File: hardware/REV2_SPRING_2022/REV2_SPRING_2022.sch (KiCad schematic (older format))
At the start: 38 parts, among them J101 Screw_Terminal_01x02, J102 Screw_Terminal_01x02, J103 Conn_01x02_Female, J104 Screw_Terminal_01x02, J105 Conn_01x02_Female, J106 Conn_01x02_Female, J107 Screw_Terminal_01x02, J108 Screw_Terminal_01x02, J109 Conn_01x02_Female, J110 Conn_01x02_Female, Q101 Q_NMOS_GDS, Q102 Q_NMOS_GDS, U1 Teensy3.6_All_Pins, U2 PA16165_Breakout, U3 MPL3115A2_Breakout, U4 BNO055_Breakout, U5 RFM69HCW_Breakout

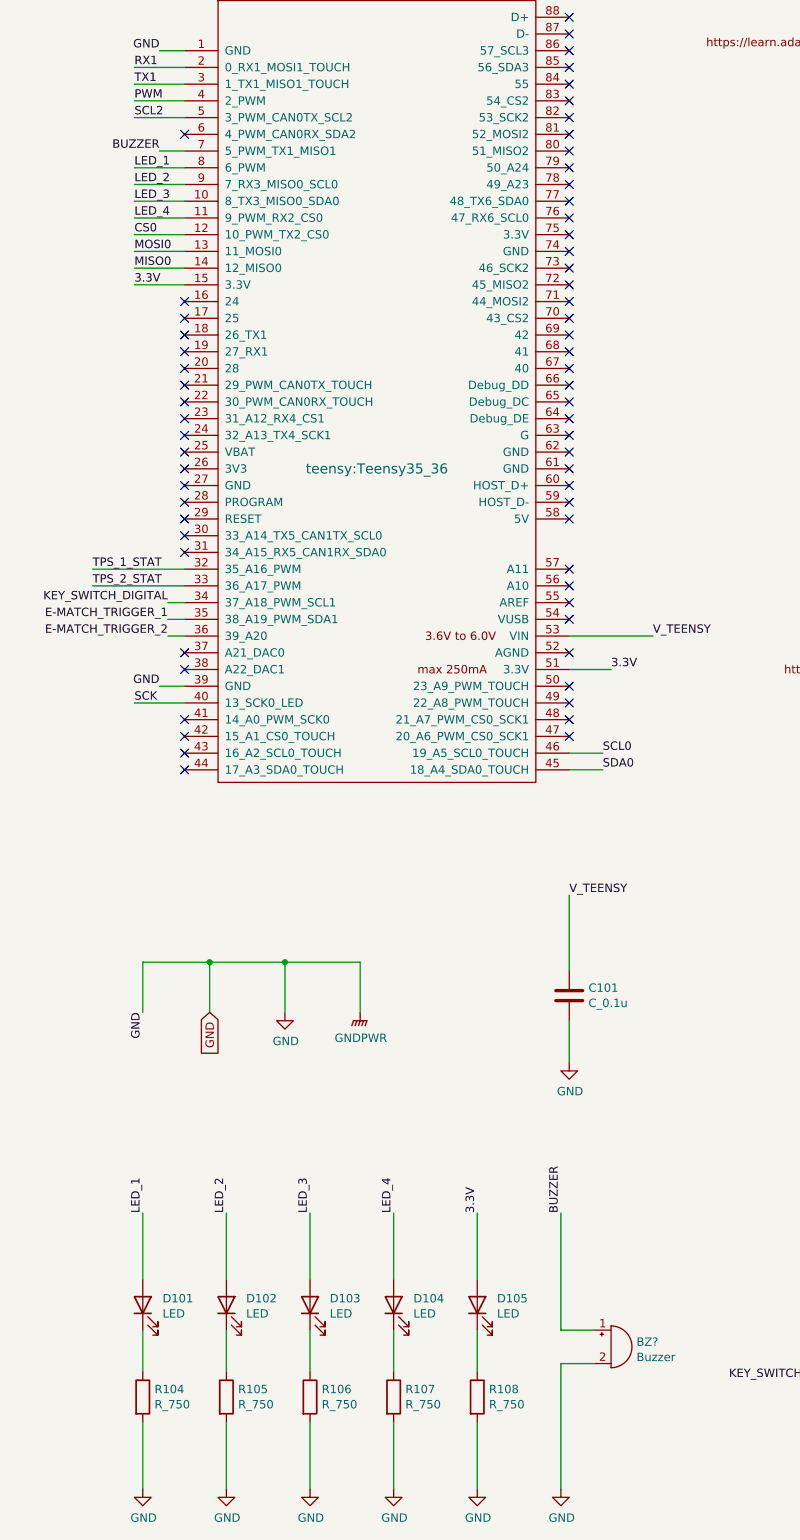
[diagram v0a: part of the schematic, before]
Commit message: add another LED to schematic and layout
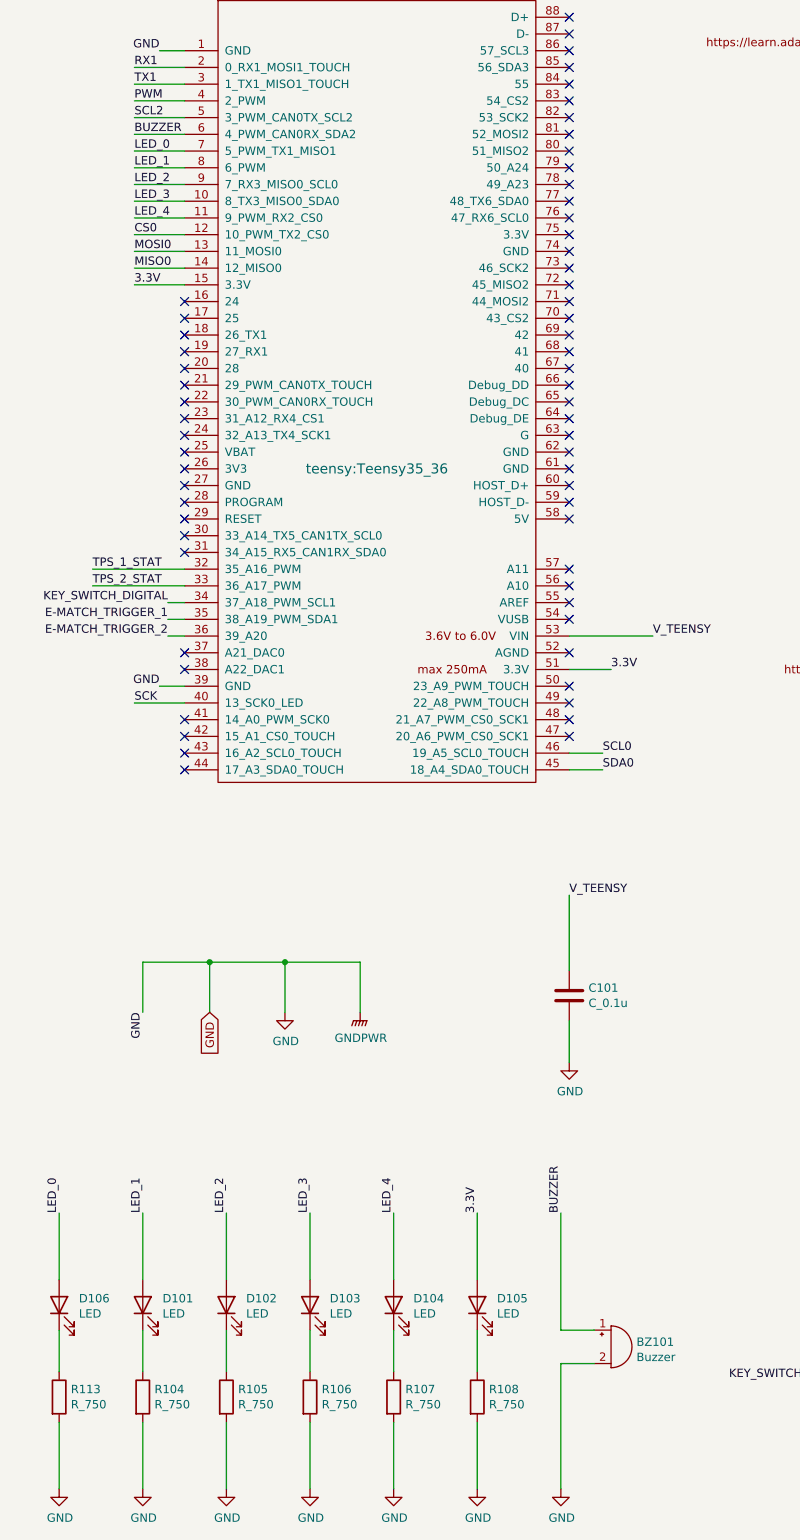
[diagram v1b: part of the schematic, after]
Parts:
- added D106: LED, LED_SMD:LED_0805_2012Metric_Pad1.15x1.40mm_HandSolder, symbol Device:LED
- added R113: R_750, Resistor_SMD:R_0805_2012Metric_Pad1.20x1.40mm_HandSolder, symbol Device:R
- gave numbers to parts that had none: 1
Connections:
- net BUZZER: now also U1.6 (4_PWM_CAN0RX_SDA2); no longer U1.7 (5_PWM_TX1_MISO1)
- net GND: now also R113.2
- new net: D106.1 (K), R113.1
- new net LED_0: D106.2 (A), U1.7 (5_PWM_TX1_MISO1)
- no-connect marks 83 -> 82
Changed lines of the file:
@@
 Wire Wire Line
 	8400 2850 8700 2850
-NoConn ~ 1450 1950
 NoConn ~ 1450 2950
 NoConn ~ 1450 3050
@@
 KEY_SWITCH_DIGITAL
 $Comp
-L Device:Buzzer BZ?
+L Device:Buzzer BZ101
 U 1 1 61F00FB7
 P 4000 9200
-F 0 "BZ?" H 4152 9229 50  0000 L CNN
+F 0 "BZ101" H 4152 9229 50  0000 L CNN
 F 1 "Buzzer" H 4152 9138 50  0000 L CNN
 F 2 "Olin_Rocketry:Large_Buzzer_24mmOD_14.8mmPinDistance_1.0mmPinDiameter" V 3975 9300 50  0001 C CNN
@@
 	3700 9300 3700 10050
 $Comp
-L power:GND #PWR?
+L power:GND #PWR0116
 U 1 1 61F0EB81
 P 3700 10050
-F 0 "#PWR?" H 3700 9800 50  0001 C CNN
+F 0 "#PWR0116" H 3700 9800 50  0001 C CNN
 F 1 "GND" H 3705 9877 50  0000 C CNN
 F 2 "" H 3700 10050 50  0001 C CNN
@@
 Text Label 3700 8400 1    50   ~ 0
 BUZZER
-Text Label 1300 2050 2    50   ~ 0
+Text Label 1150 1950 0    50   ~ 0
 BUZZER
 Wire Wire Line
-	1450 2050 1300 2050
+	1450 2050 1150 2050
+$Comp
+L Device:LED D106
+U 1 1 61F1A35A
+P 700 8950
+F 0 "D106" V 739 8832 50  0000 R CNN
+F 1 "LED" V 648 8832 50  0000 R CNN
+F 2 "LED_SMD:LED_0805_2012Metric_Pad1.15x1.40mm_HandSolder" H 700 8950 50  0001 C CNN
+F 3 "https://datasheet.lcsc.com/lcsc/1806130620_Hubei-KENTO-Elec-C2293_C2293.pdf" H 700 8950 50  0001 C CNN
+	1    700  8950
+	0    -1   -1   0
+$EndComp
+$Comp
+L Device:R R113
+U 1 1 61F1A360
+P 700 9500
+F 0 "R113" H 770 9546 50  0000 L CNN
+F 1 "R_750" H 770 9455 50  0000 L CNN
+F 2 "Resistor_SMD:R_0805_2012Metric_Pad1.20x1.40mm_HandSolder" V 630 9500 50  0001 C CNN
+F 3 "~" H 700 9500 50  0001 C CNN
+	1    700  9500
+	1    0    0    -1
+$EndComp
+Wire Wire Line
+	700  9100 700  9350
+Text Label 700  8400 1    50   ~ 0
+LED_0
+Wire Wire Line
+	700  8400 700  8800
+Wire Wire Line
+	700  9650 700  10050
+$Comp
+L power:GND #PWR0122
+U 1 1 61F1A36A
+P 700 10050
+F 0 "#PWR0122" H 700 9800 50  0001 C CNN
+F 1 "GND" H 705 9877 50  0000 C CNN
+F 2 "" H 700 10050 50  0001 C CNN
+F 3 "" H 700 10050 50  0001 C CNN
+	1    700  10050
+	1    0    0    -1
+$EndComp
+Text Label 1150 2050 0    50   ~ 0
+LED_0
+Wire Wire Line
+	1450 1950 1150 1950
 $EndSCHEMATC

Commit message: wip
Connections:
- net EMATCH_1+: now reaches J101.2 (Pin_2), J109.2 (Pin_2), Q101.2 (D), R111.2
- net EMATCH_2+: now reaches J102.2 (Pin_2), J110.2 (Pin_2), Q102.2 (D), R112.2
- net TPS2113A for E-match/IN1 renamed BAT1
- net TPS2113A for E-match/IN2 renamed BAT2
- net TPS2113A for E-match/VOUT renamed V_EMATCH_TO_KEY_SWITCH
- net TPS2113A for Teensy power/VOUT renamed VIN_TO_TEENSY_TO_KEY_SWITCH
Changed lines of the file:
@@
 Wire Wire Line
 	1450 1950 1150 1950
+Text Label 21050 3200 0    50   ~ 0
+EMATCH_1+
+Text Label 21050 6200 0    50   ~ 0
+EMATCH_2+
+Text Label 6250 8950 0    50   ~ 0
+KEY_SWITCH_DIGITAL_3V3
+Text Label 16250 2700 0    50   ~ 0
+V_EMATCH_TO_KEY_SWITCH
+Text Label 16200 5050 0    50   ~ 0
+VIN_TO_TEENSY_TO_KEY_SWITCH
+Text Label 13400 4350 0    50   ~ 0
+BAT1
+Text Label 13400 3500 0    50   ~ 0
+BAT2
 $EndSCHEMATC

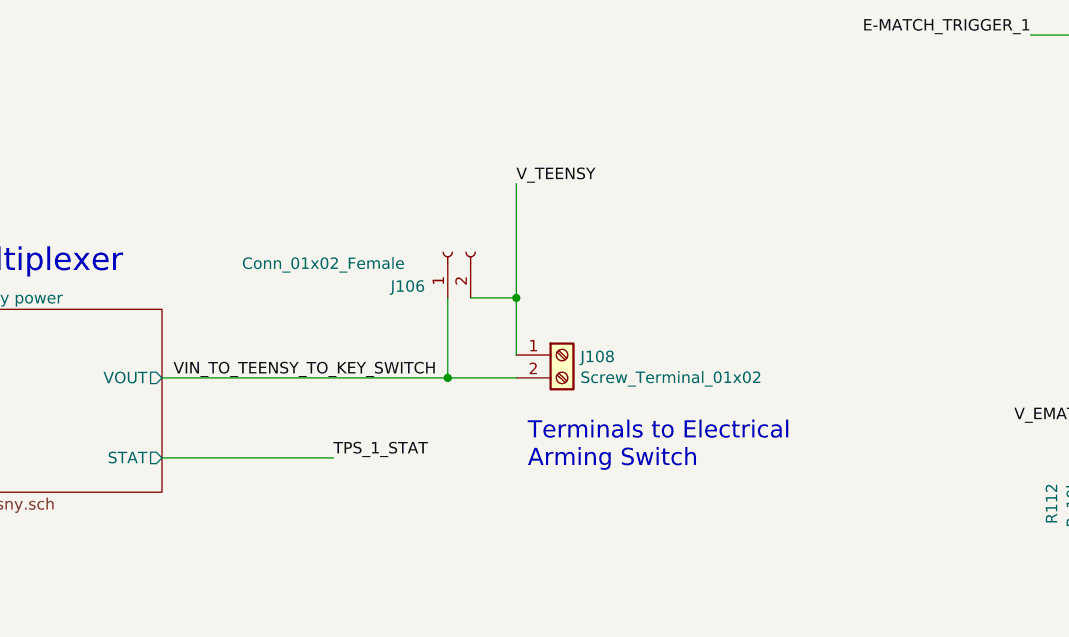
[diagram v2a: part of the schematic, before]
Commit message: remove hardware electrical arming (now using software arming)
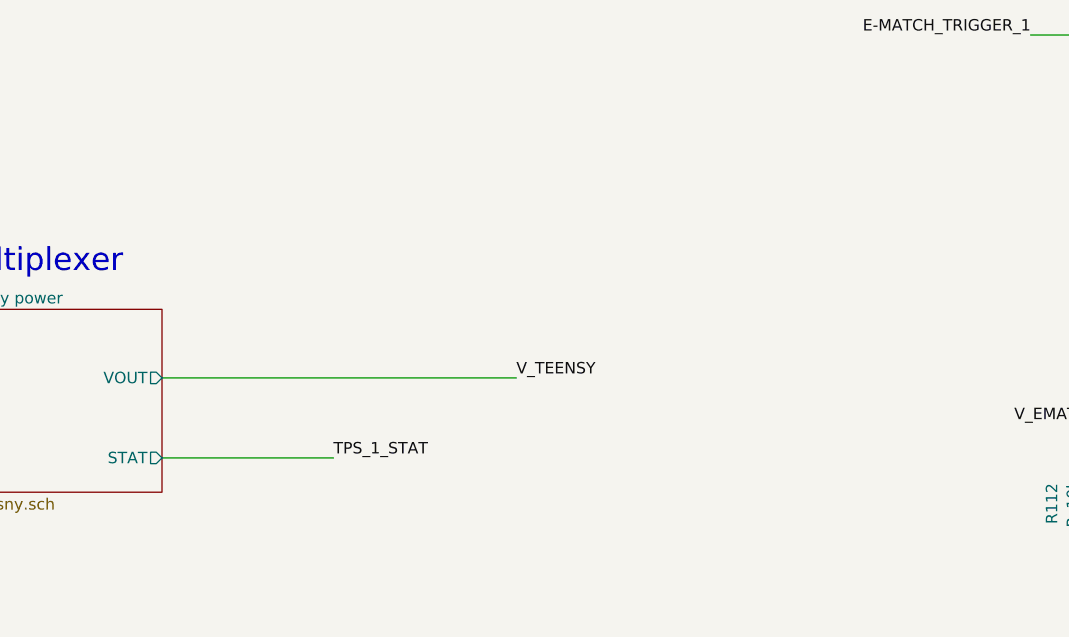
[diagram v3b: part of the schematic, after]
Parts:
- removed J106: Conn_01x02_Female, Connector_Wire:SolderWire-1sqmm_1x02_P5.4mm_D1.4mm_OD2.7mm_Relief2x, symbol Connector:Conn_01x02_Female
- removed J108: Screw_Terminal_01x02, TerminalBlock:TerminalBlock_bornier-2_P5.08mm, symbol Connector:Screw_Terminal_01x02
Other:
- note removed: "Terminals to Electrical \nArming Switch"
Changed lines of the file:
@@
 	0    1    1    0
 $EndComp
-Text Label 17700 4200 0    50   ~ 0
+Text Label 17700 5050 0    50   ~ 0
 V_TEENSY
 Text Label 17700 2050 0    50   ~ 0
@@
 Text Notes 17750 3050 0    75   ~ 0
 Terminals to Electromechanical \nArming Switch
-$Comp
-L Connector:Screw_Terminal_01x02 J108
-U 1 1 61BB7A24
-P 17900 4950
-F 0 "J108" H 17980 4942 50  0000 L CNN
-F 1 "Screw_Terminal_01x02" H 17980 4851 50  0000 L CNN
-F 2 "TerminalBlock:TerminalBlock_bornier-2_P5.08mm" H 17900 4950 50  0001 C CNN
-F 3 "~" H 17900 4950 50  0001 C CNN
-	1    17900 4950
-	1    0    0    -1
-$EndComp
-Wire Wire Line
-	16150 5050 17400 5050
-Wire Wire Line
-	17700 4950 17700 4700
-Text Notes 17750 5450 0    75   ~ 0
-Terminals to Electrical \nArming Switch
 Text Notes 14700 2250 0    100  ~ 0
 Power Multiplexer
@@
 	17400 2700 17700 2700
 $Comp
-L Connector:Conn_01x02_Female J106
-U 1 1 61EF490E
-P 17400 4500
-F 0 "J106" V 17250 4750 50  0000 R CNN
-F 1 "Conn_01x02_Female" V 17350 5400 50  0000 R CNN
-F 2 "Connector_Wire:SolderWire-1sqmm_1x02_P5.4mm_D1.4mm_OD2.7mm_Relief2x" H 17400 4500 50  0001 C CNN
-F 3 "~" H 17400 4500 50  0001 C CNN
-	1    17400 4500
-	0    -1   -1   0
-$EndComp
-Wire Wire Line
-	17500 4700 17700 4700
-Connection ~ 17700 4700
-Wire Wire Line
-	17700 4700 17700 4200
-Wire Wire Line
-	17400 4700 17400 5050
-Connection ~ 17400 5050
-Wire Wire Line
-	17400 5050 17700 5050
-$Comp
 L Device:R R111
 U 1 1 61EFFA45
@@
 Text Label 16250 2700 0    50   ~ 0
 V_EMATCH_TO_KEY_SWITCH
-Text Label 16200 5050 0    50   ~ 0
-VIN_TO_TEENSY_TO_KEY_SWITCH
 Text Label 13400 4350 0    50   ~ 0
 BAT1
 Text Label 13400 3500 0    50   ~ 0
 BAT2
+Wire Wire Line
+	16150 5050 17700 5050
 $EndSCHEMATC

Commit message: wip switch wire terminals
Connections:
- net EMATCH_1+: now also J101.1 (Pin_1), J109.1 (Pin_1); no longer J101.2 (Pin_2), J109.2 (Pin_2)
- net EMATCH_2+: now also J102.1 (Pin_1), J110.1 (Pin_1); no longer J102.2 (Pin_2), J110.2 (Pin_2)
- net V_EMATCH: now also J101.2 (Pin_2), J102.2 (Pin_2), J107.2 (Pin_2), J109.2 (Pin_2), J110.2 (Pin_2); no longer J101.1 (Pin_1), J102.1 (Pin_1), J107.1 (Pin_1), J109.1 (Pin_1), J110.1 (Pin_1)
- net V_EMATCH_TO_KEY_SWITCH: now also J107.1 (Pin_1); no longer J107.2 (Pin_2)
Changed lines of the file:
@@
 L Connector:Screw_Terminal_01x02 J102
 U 1 1 619F16C4
-P 21750 5600
-F 0 "J102" H 21830 5592 50  0000 L CNN
-F 1 "Screw_Terminal_01x02" H 21830 5501 50  0000 L CNN
-F 2 "TerminalBlock:TerminalBlock_bornier-2_P5.08mm" H 21750 5600 50  0001 C CNN
-F 3 "~" H 21750 5600 50  0001 C CNN
-	1    21750 5600
-	1    0    0    -1
+P 21750 5700
+F 0 "J102" H 21830 5692 50  0000 L CNN
+F 1 "Screw_Terminal_01x02" H 21830 5601 50  0000 L CNN
+F 2 "TerminalBlock:TerminalBlock_bornier-2_P5.08mm" H 21750 5700 50  0001 C CNN
+F 3 "~" H 21750 5700 50  0001 C CNN
+	1    21750 5700
+	1    0    0    1
 $EndComp
 Wire Wire Line
@@
 L Connector:Screw_Terminal_01x02 J107
 U 1 1 61BAEBD9
-P 17900 2600
-F 0 "J107" H 17980 2592 50  0000 L CNN
-F 1 "Screw_Terminal_01x02" H 17980 2501 50  0000 L CNN
-F 2 "TerminalBlock:TerminalBlock_bornier-2_P5.08mm" H 17900 2600 50  0001 C CNN
-F 3 "~" H 17900 2600 50  0001 C CNN
-	1    17900 2600
-	1    0    0    -1
+P 17900 2700
+F 0 "J107" H 17980 2692 50  0000 L CNN
+F 1 "Screw_Terminal_01x02" H 17980 2601 50  0000 L CNN
+F 2 "TerminalBlock:TerminalBlock_bornier-2_P5.08mm" H 17900 2700 50  0001 C CNN
+F 3 "~" H 17900 2700 50  0001 C CNN
+	1    17900 2700
+	1    0    0    1
 $EndComp
 Wire Wire Line
@@
 Wire Wire Line
 	14350 3050 14700 3050
-$Comp
-L Connector:Conn_01x02_Female J105
-U 1 1 61EE6B30
-P 17400 2150
-F 0 "J105" V 17250 2400 50  0000 R CNN
-F 1 "Conn_01x02_Female" V 17350 3050 50  0000 R CNN
-F 2 "Connector_Wire:SolderWire-1sqmm_1x02_P5.4mm_D1.4mm_OD2.7mm_Relief2x" H 17400 2150 50  0001 C CNN
-F 3 "~" H 17400 2150 50  0001 C CNN
-	1    17400 2150
-	0    -1   -1   0
-$EndComp
 Wire Wire Line
 	17500 2350 17700 2350
@@
 L Connector:Conn_01x02_Female J110
 U 1 1 61F21E7F
-P 21600 5150
-F 0 "J110" V 21450 4850 50  0000 R CNN
-F 1 "Conn_01x02_Female" V 21600 4850 50  0000 R CNN
-F 2 "Connector_Wire:SolderWire-1sqmm_1x02_P5.4mm_D1.4mm_OD2.7mm_Relief2x" H 21600 5150 50  0001 C CNN
-F 3 "~" H 21600 5150 50  0001 C CNN
-	1    21600 5150
-	0    -1   -1   0
+P 21700 5150
+F 0 "J110" V 21600 5400 50  0000 R CNN
+F 1 "Conn_01x02_Female" V 21700 6000 50  0000 R CNN
+F 2 "Connector_Wire:SolderWire-1sqmm_1x02_P5.4mm_D1.4mm_OD2.7mm_Relief2x" H 21700 5150 50  0001 C CNN
+F 3 "~" H 21700 5150 50  0001 C CNN
+	1    21700 5150
+	0    1    -1   0
 $EndComp
 Wire Wire Line
@@
 L Connector:Conn_01x02_Female J109
 U 1 1 61F16DD4
-P 21600 2150
-F 0 "J109" V 21450 1850 50  0000 R CNN
-F 1 "Conn_01x02_Female" V 21600 1850 50  0000 R CNN
-F 2 "Connector_Wire:SolderWire-1sqmm_1x02_P5.4mm_D1.4mm_OD2.7mm_Relief2x" H 21600 2150 50  0001 C CNN
-F 3 "~" H 21600 2150 50  0001 C CNN
-	1    21600 2150
-	0    -1   -1   0
+P 21700 2150
+F 0 "J109" V 21550 2400 50  0000 R CNN
+F 1 "Conn_01x02_Female" V 21700 3000 50  0000 R CNN
+F 2 "Connector_Wire:SolderWire-1sqmm_1x02_P5.4mm_D1.4mm_OD2.7mm_Relief2x" H 21700 2150 50  0001 C CNN
+F 3 "~" H 21700 2150 50  0001 C CNN
+	1    21700 2150
+	0    1    -1   0
 $EndComp
 Connection ~ 21050 3050
@@
 L Connector:Screw_Terminal_01x02 J101
 U 1 1 61A64E05
-P 21750 2600
-F 0 "J101" H 21830 2592 50  0000 L CNN
-F 1 "Screw_Terminal_01x02" H 21830 2501 50  0000 L CNN
-F 2 "TerminalBlock:TerminalBlock_bornier-2_P5.08mm" H 21750 2600 50  0001 C CNN
-F 3 "~" H 21750 2600 50  0001 C CNN
-	1    21750 2600
-	1    0    0    -1
+P 21750 2700
+F 0 "J101" H 21830 2692 50  0000 L CNN
+F 1 "Screw_Terminal_01x02" H 21830 2601 50  0000 L CNN
+F 2 "TerminalBlock:TerminalBlock_bornier-2_P5.08mm" H 21750 2700 50  0001 C CNN
+F 3 "~" H 21750 2700 50  0001 C CNN
+	1    21750 2700
+	1    0    0    1
 $EndComp
 Connection ~ 21450 2700
@@
 Wire Wire Line
 	16150 5050 17700 5050
+$Comp
+L Connector:Conn_01x02_Female J105
+U 1 1 61EE6B30
+P 17400 2150
+F 0 "J105" V 17250 2400 50  0000 R CNN
+F 1 "Conn_01x02_Female" V 17350 3050 50  0000 R CNN
+F 2 "Connector_Wire:SolderWire-1sqmm_1x02_P5.4mm_D1.4mm_OD2.7mm_Relief2x" H 17400 2150 50  0001 C CNN
+F 3 "~" H 17400 2150 50  0001 C CNN
+	1    17400 2150
+	0    -1   -1   0
+$EndComp
 $EndSCHEMATC

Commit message: wip
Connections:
- net V_EMATCH: now also J105.1 (Pin_1), J107.1 (Pin_1); no longer J105.2 (Pin_2), J107.2 (Pin_2)
- net V_EMATCH_TO_KEY_SWITCH: now also J105.2 (Pin_2), J107.2 (Pin_2); no longer J105.1 (Pin_1), J107.1 (Pin_1)
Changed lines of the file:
@@
 L Connector:Screw_Terminal_01x02 J107
 U 1 1 61BAEBD9
-P 17900 2700
-F 0 "J107" H 17980 2692 50  0000 L CNN
-F 1 "Screw_Terminal_01x02" H 17980 2601 50  0000 L CNN
-F 2 "TerminalBlock:TerminalBlock_bornier-2_P5.08mm" H 17900 2700 50  0001 C CNN
-F 3 "~" H 17900 2700 50  0001 C CNN
-	1    17900 2700
-	1    0    0    1
+P 17900 2600
+F 0 "J107" H 17980 2592 50  0000 L CNN
+F 1 "Screw_Terminal_01x02" H 17980 2501 50  0000 L CNN
+F 2 "TerminalBlock:TerminalBlock_bornier-2_P5.08mm" H 17900 2600 50  0001 C CNN
+F 3 "~" H 17900 2600 50  0001 C CNN
+	1    17900 2600
+	1    0    0    -1
 $EndComp
 Wire Wire Line
@@
 L Connector:Conn_01x02_Female J105
 U 1 1 61EE6B30
-P 17400 2150
-F 0 "J105" V 17250 2400 50  0000 R CNN
-F 1 "Conn_01x02_Female" V 17350 3050 50  0000 R CNN
-F 2 "Connector_Wire:SolderWire-1sqmm_1x02_P5.4mm_D1.4mm_OD2.7mm_Relief2x" H 17400 2150 50  0001 C CNN
-F 3 "~" H 17400 2150 50  0001 C CNN
-	1    17400 2150
-	0    -1   -1   0
+P 17500 2150
+F 0 "J105" V 17400 1950 50  0000 R CNN
+F 1 "Conn_01x02_Female" V 17500 1950 50  0000 R CNN
+F 2 "Connector_Wire:SolderWire-1sqmm_1x02_P5.4mm_D1.4mm_OD2.7mm_Relief2x" H 17500 2150 50  0001 C CNN
+F 3 "~" H 17500 2150 50  0001 C CNN
+	1    17500 2150
+	0    1    -1   0
 $EndComp
 $EndSCHEMATC
